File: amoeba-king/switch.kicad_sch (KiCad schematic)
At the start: 2 parts

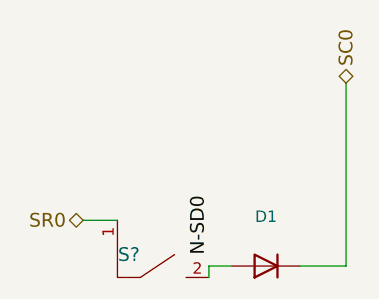
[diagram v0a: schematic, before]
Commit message: Migrate Amoeba King to KiCad 10, bundle 3D models, and fix DRC/ERC
- Convert schematics and PCB to KiCad 10 format
- Add bundled local 3D models with relative ${KIPRJMOD} paths (Switch, Kailh socket, DSA keycap, SK6812 MINI-E, SOD-123 diode)
- Bundle and reference all symbols and footprints locally in amoeba-modules
- Fix dangling track, missing junctions, and net connections
- Configure board and schematic design rules for 0 DRC and 0 ERC violations
- Update Makefile for kicad-cli DRC, ERC, and Gerber export
- Remove obsolete legacy KiCad 4/5 files
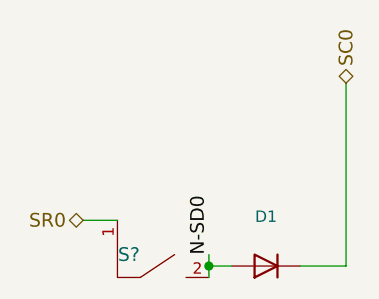
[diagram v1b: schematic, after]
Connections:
- net N-SD0: now also D1.2 (A), S?.2
